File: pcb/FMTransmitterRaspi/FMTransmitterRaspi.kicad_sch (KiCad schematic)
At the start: 32 parts, among them J1 GPIO, J2 Line In/Out, J3 Antenna, J4 GPIO, J5 External PSU 5V, U1 PCM5102A, U2 QN8072, U3 ME6211C33M5, Y1 12MHz

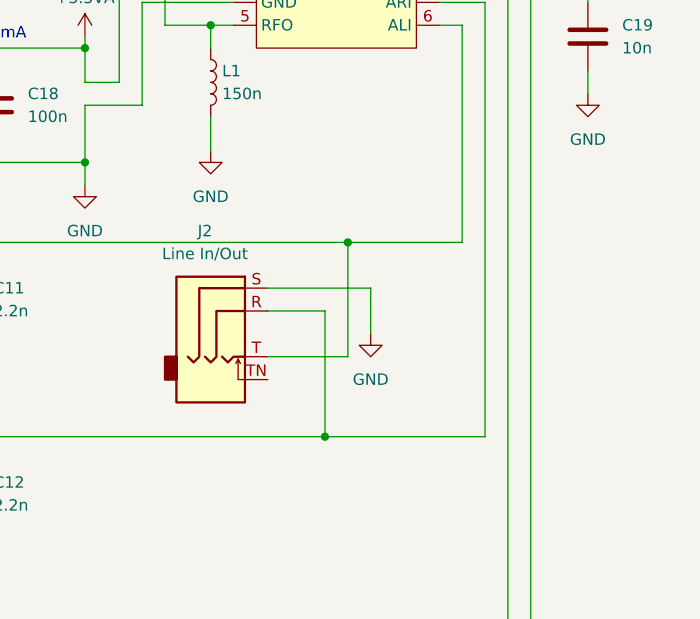
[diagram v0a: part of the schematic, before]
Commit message: Added DC blocking caps at the QN8027 input
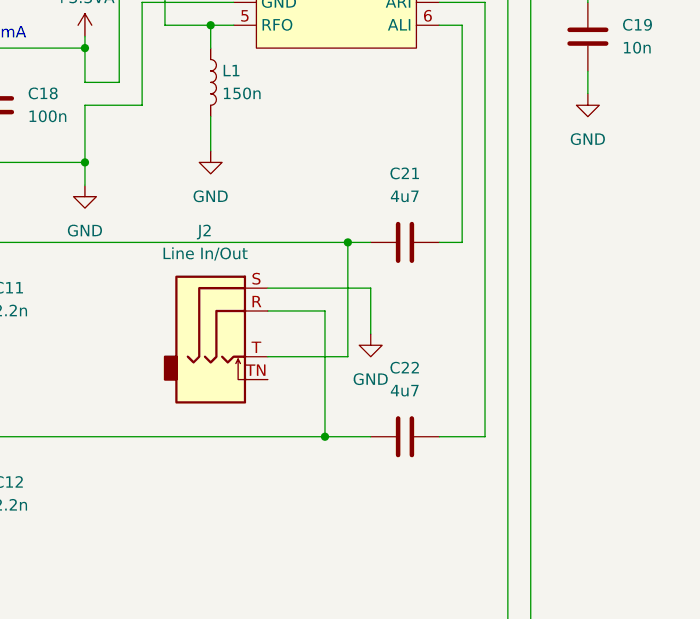
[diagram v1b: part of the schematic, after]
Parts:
- added C21, C22: 4u7, symbol Device:C
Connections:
- net at C12.1, J2.R, R2.2: now also C22.1; no longer U2.7 (ARI)
- net at C11.1, J2.T, R1.2: now also C21.1; no longer U2.6 (ALI)
- new net: C22.2, U2.7 (ARI)
- new net: C21.2, U2.6 (ALI)
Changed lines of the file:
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@@
 	)
 	(junction
-		(at 229.87 115.57)
-		(diameter 0)
-		(color 0 0 0 0)
-	)
-	(junction
 		(at 76.2 68.58)
 		(diameter 1.016)
@@
 	)
 	(junction
+		(at 229.87 115.57)
+		(diameter 0)
+		(color 0 0 0 0)
+	)
+	(junction
 		(at 165.1 27.94)
 		(diameter 1.016)
@@
 	)
 	(junction
-		(at 227.33 137.16)
-		(diameter 0)
-		(color 0 0 0 0)
-	)
-	(junction
 		(at 58.42 58.42)
 		(diameter 1.016)
@@
 	)
 	(junction
+		(at 227.33 137.16)
+		(diameter 0)
+		(color 0 0 0 0)
+	)
+	(junction
 		(at 76.2 50.8)
 		(diameter 1.016)
@@
 	(wire
 		(pts
+			(xy 227.33 137.16) (xy 232.41 137.16)
+		)
+		(stroke
+			(width 0)
+			(type default)
+		)
+	)
+	(wire
+		(pts
 			(xy 60.96 40.64) (xy 31.75 40.64)
 		)
@@
 	(wire
 		(pts
-			(xy 229.87 115.57) (xy 242.57 115.57)
-		)
-		(stroke
-			(width 0)
-			(type default)
-		)
-	)
-	(wire
-		(pts
 			(xy 152.4 93.98) (xy 152.4 96.52)
 		)
@@
 	(wire
 		(pts
-			(xy 227.33 137.16) (xy 245.11 137.16)
-		)
-		(stroke
-			(width 0)
-			(type default)
-		)
-	)
-	(wire
-		(pts
 			(xy 73.66 40.64) (xy 109.22 40.64)
 		)
@@
 	(wire
 		(pts
+			(xy 240.03 115.57) (xy 242.57 115.57)
+		)
+		(stroke
+			(width 0)
+			(type default)
+		)
+	)
+	(wire
+		(pts
 			(xy 217.17 83.82) (xy 212.09 83.82)
 		)
@@
 	(wire
 		(pts
+			(xy 229.87 115.57) (xy 232.41 115.57)
+		)
+		(stroke
+			(width 0)
+			(type default)
+		)
+	)
+	(wire
+		(pts
 			(xy 245.11 137.16) (xy 245.11 88.9)
 		)
@@
 	(wire
 		(pts
+			(xy 240.03 137.16) (xy 245.11 137.16)
+		)
+		(stroke
+			(width 0)
+			(type default)
+		)
+	)
+	(wire
+		(pts
 			(xy 127 107.95) (xy 127 110.49)
 		)
@@
 	(symbol
 		(lib_id "Device:C")
+		(at 236.22 137.16 90)
+		(unit 1)
+		(body_style 1)
+		(exclude_from_sim no)
+		(in_bom yes)
+		(on_board yes)
+		(in_pos_files yes)
+		(dnp no)
+		(fields_autoplaced yes)
+		(property "Reference" "C22"
+			(at 236.22 129.54 90)
+			(show_name no)
+			(do_not_autoplace no)
+			(effects
+				(font
+					(size 1.27 1.27)
+				)
+			)
+		)
+		(property "Value" "4u7"
+			(at 236.22 132.08 90)
+			(show_name no)
+			(do_not_autoplace no)
+			(effects
+				(font
+					(size 1.27 1.27)
+				)
+			)
+		)
+		(property "Footprint" ""
+			(at 240.03 136.1948 0)
+			(hide yes)
+			(show_name no)
+			(do_not_autoplace no)
+			(effects
+				(font
+					(size 1.27 1.27)
+				)
+			)
+		)
+		(property "Datasheet" ""
+			(at 236.22 137.16 0)
+			(hide yes)
+			(show_name no)
+			(do_not_autoplace no)
+			(effects
+				(font
+					(size 1.27 1.27)
+				)
+			)
+		)
+		(property "Description" "Unpolarized capacitor"
+			(at 236.22 137.16 0)
+			(hide yes)
+			(show_name no)
+			(do_not_autoplace no)
+			(effects
+				(font
+					(size 1.27 1.27)
+				)
+			)
+		)
+		(pin "1"
+		)
+		(pin "2"
+		)
+		(instances
+			(project "FMTransmitterRaspi"
+				(path "/e63e39d7-6ac0-4ffd-8aa3-1841a4541b55"
+					(reference "C22")
+					(unit 1)
+				)
+			)
+		)
+	)
+	(symbol
+		(lib_id "Device:C")
 		(at 123.19 180.34 0)
 		(unit 1)
@@
 					(unit 1)
 				)
+			)
+		)
+	)
+	(symbol
+		(lib_id "Device:C")
+		(at 236.22 115.57 90)
+		(unit 1)
+		(body_style 1)
+		(exclude_from_sim no)
+		(in_bom yes)
+		(on_board yes)
+		(in_pos_files yes)
+		(dnp no)
+		(fields_autoplaced yes)
+		(property "Reference" "C21"
+			(at 236.22 107.95 90)
+			(show_name no)
+			(do_not_autoplace no)
+			(effects
+				(font
+					(size 1.27 1.27)
+				)
+			)
+		)
+		(property "Value" "4u7"
+			(at 236.22 110.49 90)
+			(show_name no)
+			(do_not_autoplace no)
+			(effects
+				(font
+					(size 1.27 1.27)
+				)
+			)
+		)
+		(property "Footprint" ""
+			(at 240.03 114.6048 0)
+			(hide yes)
+			(show_name no)
+			(do_not_autoplace no)
+			(effects
+				(font
+					(size 1.27 1.27)
+				)
+			)
+		)
+		(property "Datasheet" ""
+			(at 236.22 115.57 0)
+			(hide yes)
+			(show_name no)
+			(do_not_autoplace no)
+			(effects
+				(font
+					(size 1.27 1.27)
+				)
+			)
+		)
+		(property "Description" "Unpolarized capacitor"
+			(at 236.22 115.57 0)
+			(hide yes)
+			(show_name no)
+			(do_not_autoplace no)
+			(effects
+				(font
+					(size 1.27 1.27)
+				)
+			)
+		)
+		(pin "2"
+		)
+		(pin "1"
+		)
+		(instances
+			(project "FMTransmitterRaspi"
+				(path "/e63e39d7-6ac0-4ffd-8aa3-1841a4541b55"
+					(reference "C21")
+					(unit 1)
+				)

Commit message: Ready for production
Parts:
- removed C7: 10u, Capacitor_SMD:C_0603_1608Metric_Pad1.08x0.95mm_HandSolder, symbol Device:C
- removed C8: 100n, Capacitor_SMD:C_0603_1608Metric_Pad1.08x0.95mm_HandSolder, symbol Device:C
- removed J3: Antenna, symbol Connector:Conn_01x01_Socket
- removed J5: External PSU 5V, symbol Connector:Screw_Terminal_01x02
- added J1: Antenna/External Power, TerminalBlock:TerminalBlock_MaiXu_MX126-5.0-03P_1x03_P5.00mm, symbol Connector:Screw_Terminal_01x03
- added J4: USB-C Power, Connector_USB:USB_C_Receptacle_HRO_TYPE-C-31-M-17, symbol Connector:USB_C_Receptacle_PowerOnly_6P
- added J6: Line In/Out 2, Connector_PinHeader_2.54mm:PinHeader_1x03_P2.54mm_Vertical, symbol Connector:Conn_01x03_Pin
- added R2: 5k1, Resistor_SMD:R_0603_1608Metric_Pad0.98x0.95mm_HandSolder, symbol Device:R
- added Y1: 24MHz, Crystal:Crystal_HC18-U_Vertical, symbol Device:Crystal
- C11: renamed from C9; value 2.2u -> 2u2
- C14: renamed from C22; value 4u7 -> 2u2; footprint (none) -> Capacitor_THT:C_Rect_L7.2mm_W6.0mm_P5.00mm
- C15: renamed from C10; value 2.2u -> 2u2
- C9: renamed from C21; value 4u7 -> 2u2; footprint (none) -> Capacitor_THT:C_Rect_L7.2mm_W6.0mm_P5.00mm
- J2: renamed from J1; footprint Connector_PinSocket_2.54mm:PinSocket_2x20_P2.54mm_Vertical -> Library:PinSocket_2x20_P2.54mm_Vertical
- J5: renamed from J2; footprint (none) -> Library:Jack_3.5mm_PJ327A_Horizontal
- Y2: renamed from Y1; footprint (none) -> Crystal:Crystal_DS15_D1.5mm_L5.0mm_Horizontal_1EP_style1
- renumbered C20 to C1, C11 to C10, C5 to C12, C6 to C13, C15 to C16, C16 to C17, C12 to C18, C1 to C19, C14 to C2, C2 to C20, C3 to C21, C4 to C22, C13 to C3, C19 to C4, C17 to C7, C18 to C8, J4 to J3, R2 to R3, U2 to U1, U1 to U2
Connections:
- net +5V: now also J1.3 (Pin_3), J4.A9 (VBUS), J4.B9 (VBUS)
- net GND: now also J1.2 (Pin_2), J4.A12 (GND), J4.B12 (GND), J4.SH (SHIELD), J6.2 (Pin_2), R2.2
- net GPIO18/PCM.CLK: now also J3.12 (Pin_12)
- net GPIO21/PCM.DOUT: now also J3.40 (Pin_40)
- net at C14.1, C18.1, J5.R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: now also J6.3 (Pin_3)
- net at C2.1, U1.2 (XTAL1): now also Y2.1, Y1.2; no longer Y2.2
- net at C10.1, C9.1, J5.T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: now also J5.TN, J6.1 (Pin_1)
- net Antenna: now reaches C1.2
- net Antenna: now also J1.1 (Pin_1)
- net at C3.1, U1.1 (XTAL2): now also Y2.2, Y1.1; no longer Y2.1
- new net: J4.A5 (CC1), J4.B5 (CC2), R2.1
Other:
- note added: "Y1 and Y2 are alternative."
- moved on the sheet: C1, C2, C3, Y2

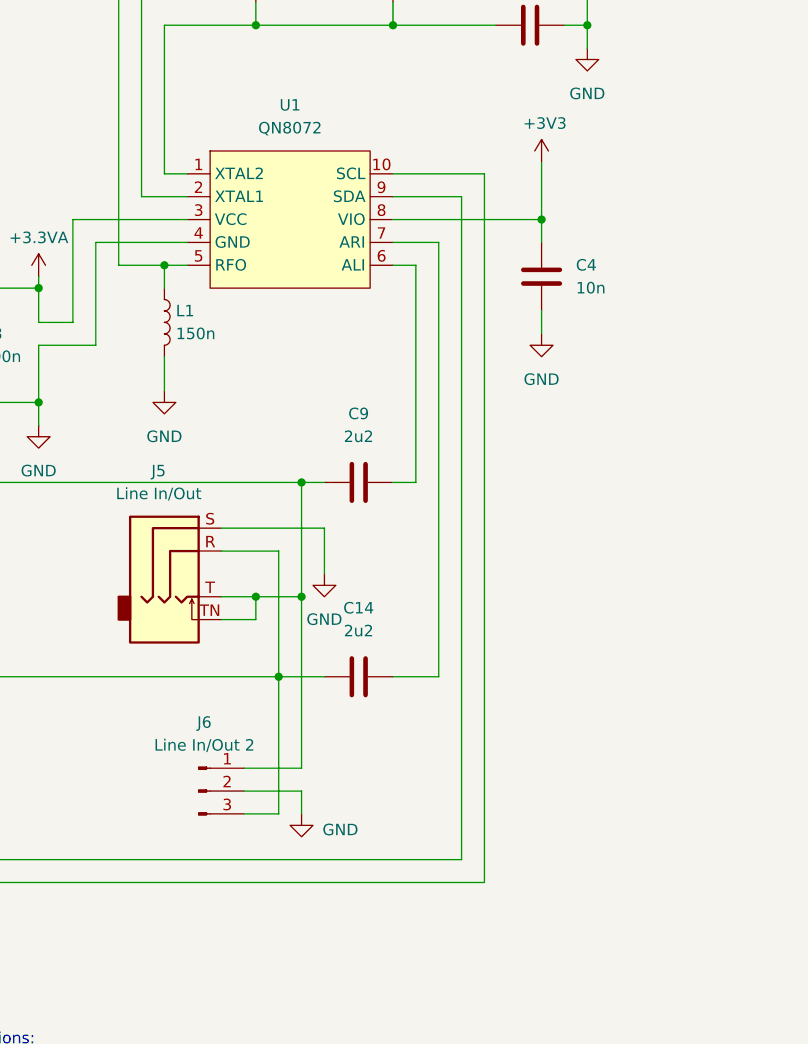
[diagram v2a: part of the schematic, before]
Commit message: corrected wrong symbol of qn8027, too wide board shape
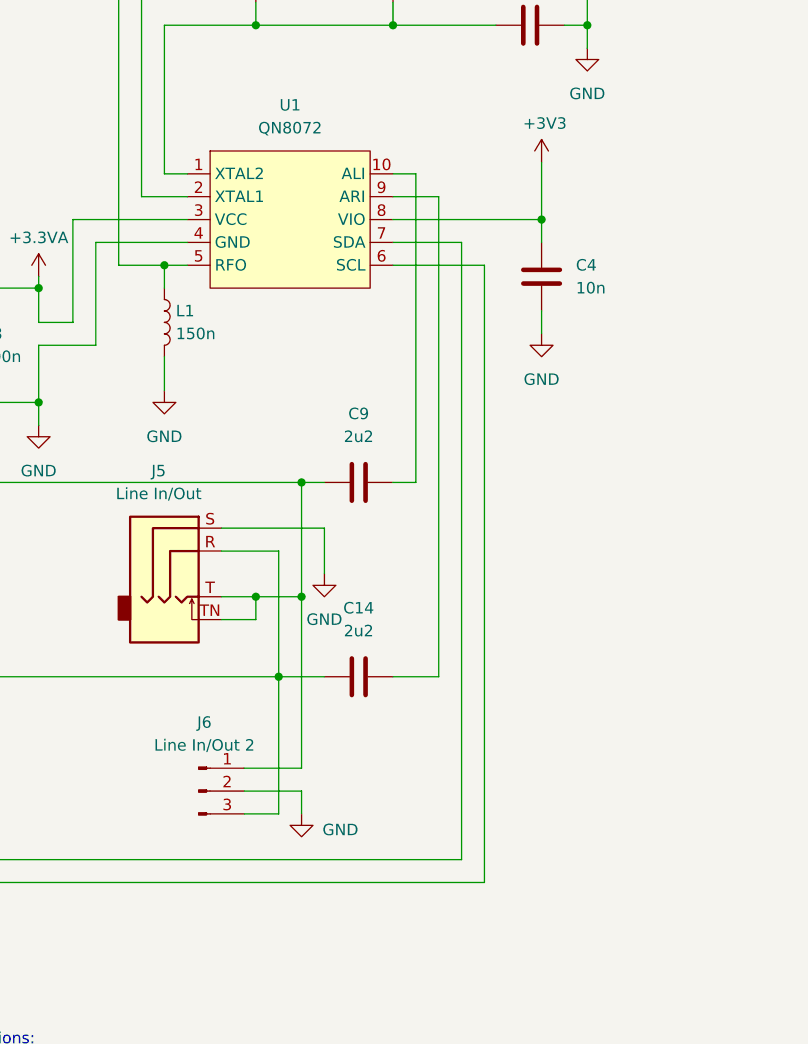
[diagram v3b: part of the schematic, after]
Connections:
- net GPIO2/SDA1: now also U1.7 (SDA); no longer U1.9 (SDA)
- net GPIO3/SCL1: now also U1.6 (SCL); no longer U1.10 (SCL)
- net at C14.2: now also U1.9 (ARI); no longer U1.7 (ARI)
- net at C9.2: now also U1.10 (ALI); no longer U1.6 (ALI)
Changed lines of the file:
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@@
-	(wire
-		(pts
-			(xy 242.57 91.44) (xy 240.03 91.44)
-		)
-		(stroke
-			(width 0)
-			(type default)
-		)
-	)
 	(wire
 		(pts
@@
 	(wire
 		(pts
+			(xy 247.65 88.9) (xy 247.65 157.48)
+		)
+		(stroke
+			(width 0)
+			(type default)
+		)
+	)
+	(wire
+		(pts
 			(xy 137.16 123.19) (xy 142.24 123.19)
 		)
@@
 	(wire
 		(pts
+			(xy 240.03 81.28) (xy 242.57 81.28)
+		)
+		(stroke
+			(width 0)
+			(type default)
+		)
+	)
+	(wire
+		(pts
 			(xy 227.33 152.4) (xy 227.33 137.16)
 		)
@@
 	(wire
 		(pts
+			(xy 240.03 91.44) (xy 250.19 91.44)
+		)
+		(stroke
+			(width 0)
+			(type default)
+		)
+	)
+	(wire
+		(pts
 			(xy 146.05 172.72) (xy 153.67 172.72)
 		)
@@
 	(wire
 		(pts
-			(xy 250.19 81.28) (xy 250.19 160.02)
-		)
-		(stroke
-			(width 0)
-			(type default)
-		)
-	)
-	(wire
-		(pts
 			(xy 165.1 27.94) (xy 162.56 27.94)
 		)
@@
 	(wire
 		(pts
-			(xy 245.11 88.9) (xy 240.03 88.9)
-		)
-		(stroke
-			(width 0)
-			(type default)
-		)
-	)
-	(wire
-		(pts
 			(xy 113.03 184.15) (xy 113.03 186.69)
 		)
@@
 	(wire
 		(pts
-			(xy 247.65 83.82) (xy 247.65 157.48)
-		)
-		(stroke
-			(width 0)
-			(type default)
-		)
-	)
-	(wire
-		(pts
 			(xy 121.92 146.05) (xy 124.46 146.05)
 		)
@@
 	(wire
 		(pts
+			(xy 240.03 88.9) (xy 247.65 88.9)
+		)
+		(stroke
+			(width 0)
+			(type default)
+		)
+	)
+	(wire
+		(pts
 			(xy 73.66 66.04) (xy 100.33 66.04)
 		)
@@
 	(wire
 		(pts
+			(xy 250.19 91.44) (xy 250.19 160.02)
+		)
+		(stroke
+			(width 0)
+			(type default)
+		)
+	)
+	(wire
+		(pts
 			(xy 69.85 123.19) (xy 69.85 127)
 		)
@@
 	(wire
 		(pts
-			(xy 242.57 115.57) (xy 242.57 91.44)
+			(xy 242.57 81.28) (xy 242.57 115.57)
 		)
 		(stroke
@@
 	(wire
 		(pts
+			(xy 240.03 83.82) (xy 245.11 83.82)
+		)
+		(stroke
+			(width 0)
+			(type default)
+		)
+	)
+	(wire
+		(pts
 			(xy 149.86 50.8) (xy 120.65 50.8)
 		)
@@
 	(wire
 		(pts
-			(xy 240.03 83.82) (xy 247.65 83.82)
-		)
-		(stroke
-			(width 0)
-			(type default)
-		)
-	)
-	(wire
-		(pts
 			(xy 261.62 64.77) (xy 261.62 67.31)
 		)
@@
 	(wire
 		(pts
-			(xy 245.11 137.16) (xy 245.11 88.9)
+			(xy 245.11 83.82) (xy 245.11 137.16)
 		)
 		(stroke
@@
 		)
 		(stroke
-			(width 0)
-			(type default)
-		)
-	)
-	(wire
-		(pts
-			(xy 240.03 81.28) (xy 250.19 81.28)
-		)
-		(stroke

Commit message: pcb beautified
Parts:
- C14, C9: value 2u2 -> 470n
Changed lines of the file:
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@@
 			)
 		)
-		(property "Value" "2u2"
+		(property "Value" "470n"
 			(at 236.22 132.08 90)
 			(show_name no)
@@
 			)
 		)
-		(property "Value" "2u2"
+		(property "Value" "470n"
 			(at 236.22 110.49 90)
 			(show_name no)

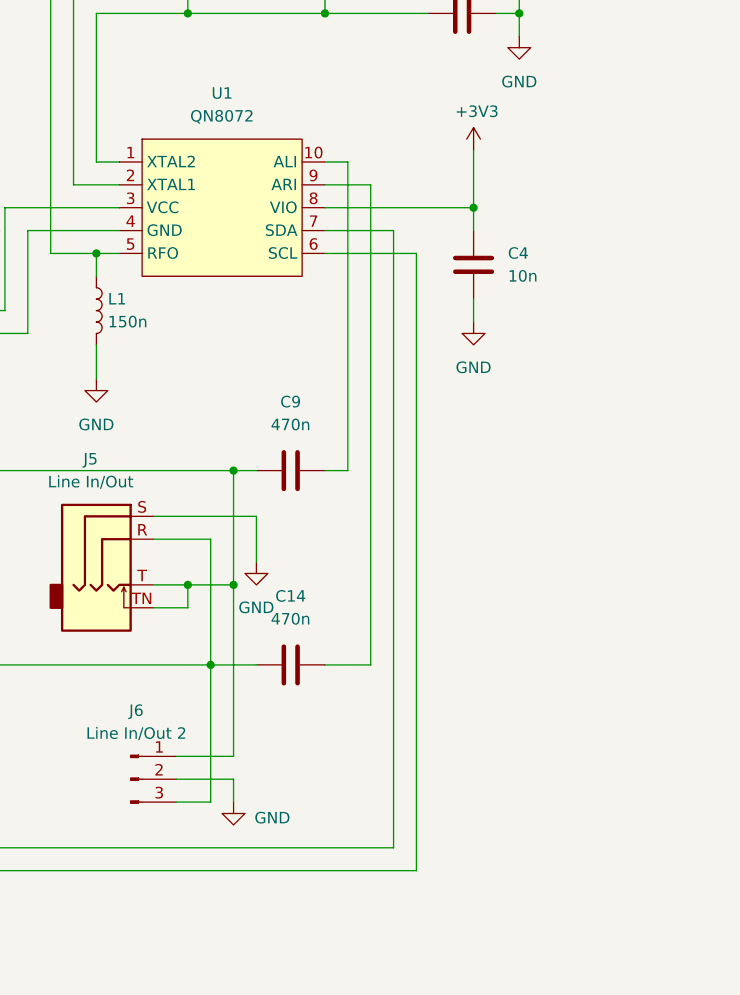
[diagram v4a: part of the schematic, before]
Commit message: added voltage divider between pcm5102 and qn8027
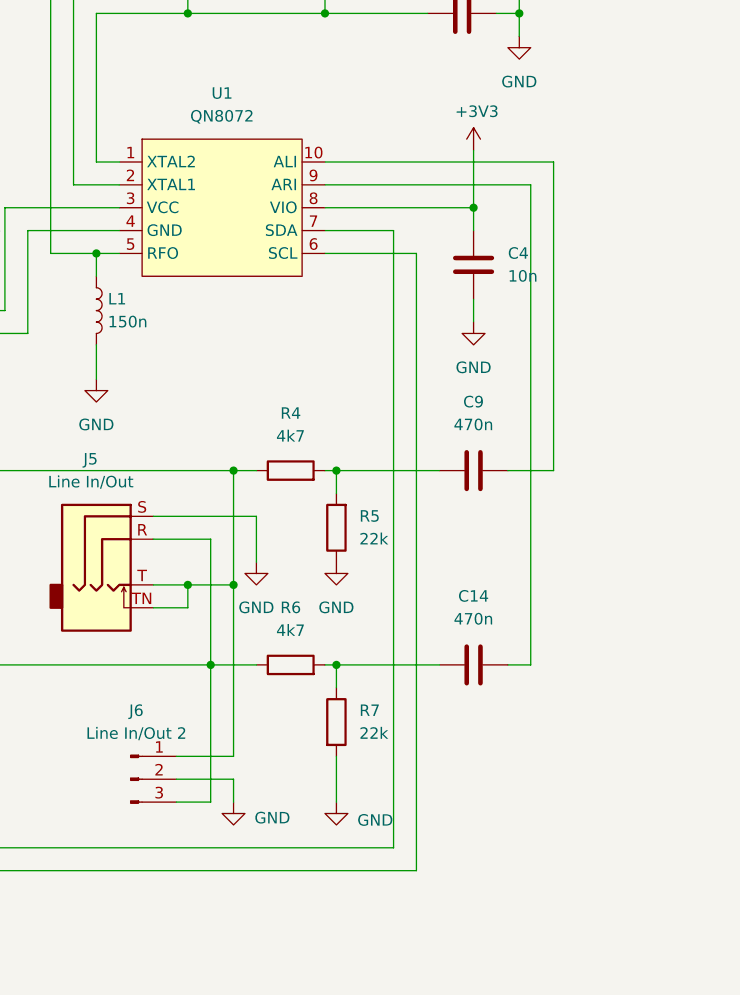
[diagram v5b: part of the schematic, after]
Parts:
- added R4, R6: 4k7, Resistor_SMD:R_0603_1608Metric_Pad0.98x0.95mm_HandSolder, symbol Device:R
- added R5, R7: 22k, Resistor_SMD:R_0603_1608Metric_Pad0.98x0.95mm_HandSolder, symbol Device:R
- C14, C9: footprint Capacitor_THT:C_Rect_L7.2mm_W6.0mm_P5.00mm -> Capacitor_THT:C_Rect_L7.2mm_W3.5mm_P5.00mm
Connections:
- net GND: now also R5.1, R7.2
- net at C18.1, J5.R, J6.3 (Pin_3)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: now also R6.1; no longer C14.1
- net at C10.1, J5.T, J5.TN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: now also R4.1; no longer C9.1
- new net: C9.1, R4.2, R5.2
- new net: C14.1, R6.2, R7.1
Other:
- moved on the sheet: C14, C9

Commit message: Werte fuer Pegelwiderstaende hinterlegt, keine weiter Aenderung
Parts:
- R4, R6: value 4k7 -> 43k
- R5, R7: value 22k -> NOT_INSTALLED
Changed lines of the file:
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@@
 		)
 	)
+	(text_box "Pegelanpassung\nR4,R6 - 43k\nR5,R7 - nicht installiert\nPassend fuer QN8027 Setting\nRin=5K, GAIN_L=0 (3db)"
+		(exclude_from_sim no)
+		(at 254.635 147.955 0)
+		(size 27.305 14.1714)
+		(margins 0.9525 0.9525 0.9525 0.9525)
+		(stroke
+			(width 0)
+			(type solid)
+		)
+		(fill
+			(type none)
+		)
+		(effects
+			(font
+				(size 1.27 1.27)
+			)
+			(justify left top)
+		)
+	)
 	(junction
 		(at 200.66 93.98)
@@
 			)
 		)
-		(property "Value" "4k7"
+		(property "Value" "43k"
 			(at 236.22 111.76 90)
 			(show_name no)
@@
 			)
 		)
-		(property "Value" "22k"
+		(property "Value" "NOT_INSTALLED"
 			(at 243.84 144.7799 0)
 			(show_name no)
@@
 			)
 		)
-		(property "Value" "4k7"
+		(property "Value" "43k"
 			(at 236.22 133.35 90)
 			(show_name no)
@@
 			)
 		)
-		(property "Value" "22k"
+		(property "Value" "NOT_INSTALLED"
 			(at 243.84 123.1899 0)
 			(show_name no)

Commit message: Rin-Wert im schematic nochmal korrigiert
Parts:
- R4, R6: value 43k -> 200k
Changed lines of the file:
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@@
 		)
 	)
-	(text_box "Pegelanpassung\nR4,R6 - 43k\nR5,R7 - nicht installiert\nPassend fuer QN8027 Setting\nRin=5K, GAIN_L=0 (3db)"
+	(text_box "Pegelanpassung\nR4,R6 - 200k\nR5,R7 - nicht installiert\nPassend fuer QN8027 Setting\nRin=10K, GAIN_L=2 (0db)"
 		(exclude_from_sim no)
 		(at 254.635 147.955 0)
@@
 			)
 		)
-		(property "Value" "43k"
+		(property "Value" "200k"
 			(at 236.22 111.76 90)
 			(show_name no)
@@
 			)
 		)
-		(property "Value" "43k"
+		(property "Value" "200k"
 			(at 236.22 133.35 90)
 			(show_name no)
